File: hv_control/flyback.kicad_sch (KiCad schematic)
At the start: 33 parts, among them Q1 FOD817A300, U30 FSL4110LR, U31 TL431MFDT

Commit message: Moving to new CCU8 implementation. Moved trace and @arm scripts to octave archive.
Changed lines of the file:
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@@
-(kicad_sch (version 20201015) (generator eeschema)
+(kicad_sch (version 20210126) (generator eeschema)
   (paper "A4")
   (junction (at 74.93 49.53) (diameter 1.016) (color 0 0 0 0))
@@
     (stroke (width 0) (type solid) (color 0 0 0 0))
   )
-  (wire (pts (xy 82.55 49.53) (xy 104.14 49.53))
-    (stroke (width 0) (type solid) (color 0 0 0 0))
-  )
   (wire (pts (xy 82.55 63.5) (xy 82.55 92.71))
     (stroke (width 0) (type solid) (color 0 0 0 0))
@@
     (stroke (width 0) (type solid) (color 0 0 0 0))
   )
+  (wire (pts (xy 104.14 49.53) (xy 82.55 49.53))
+    (stroke (width 0) (type solid) (color 0 0 0 0))
+  )
   (wire (pts (xy 104.14 49.53) (xy 104.14 53.34))
     (stroke (width 0) (type solid) (color 0 0 0 0))
@@
     (stroke (width 0) (type solid) (color 0 0 0 0))
   )
-  (wire (pts (xy 196.85 143.51) (xy 209.55 143.51))
-    (stroke (width 0) (type solid) (color 0 0 0 0))
-  )
   (wire (pts (xy 200.66 49.53) (xy 195.58 49.53))
     (stroke (width 0) (type solid) (color 0 0 0 0))
@@
   )
   (wire (pts (xy 209.55 59.69) (xy 223.52 59.69))
+    (stroke (width 0) (type solid) (color 0 0 0 0))
+  )
+  (wire (pts (xy 209.55 143.51) (xy 196.85 143.51))
     (stroke (width 0) (type solid) (color 0 0 0 0))
   )
@@
       (effects (font (size 1.524 1.524)) hide)
     )
+    (pin "1")
+    (pin "2")
   )
   (symbol (lib_id "Device:R") (at 125.73 77.47 0) (unit 1)
@@
       (effects (font (size 1.27 1.27)) hide)
     )
+    (pin "1")
+    (pin "2")
   )
   (symbol (lib_id "Local:DIODE") (at 104.14 58.42 270) (mirror x) (unit 1)
@@
       (effects (font (size 1.27 1.27)) hide)
     )
+    (pin "A")
+    (pin "C")
   )
   (symbol (lib_id "Local:DIODE") (at 125.73 91.44 270) (unit 1)
@@
       (effects (font (size 1.27 1.27)) hide)
     )
+    (pin "A")
+    (pin "C")
   )
   (symbol (lib_id "Local:DIODE") (at 186.69 49.53 0) (unit 1)
@@
       (effects (font (size 1.524 1.524)) hide)
     )
+    (pin "A")
+    (pin "C")
   )
   (symbol (lib_id "Local:DIODE") (at 186.69 74.93 0) (mirror y) (unit 1)
@@
       (effects (font (size 1.524 1.524)) hide)
     )
+    (pin "A")
+    (pin "C")
   )
   (symbol (lib_id "Local:R") (at 74.93 57.15 0) (unit 1)
@@
       (effects (font (size 1.27 1.27)) hide)
     )
+    (pin "1")
+    (pin "2")
   )
   (symbol (lib_id "Local:R") (at 74.93 109.22 0) (unit 1)
@@
       (effects (font (size 1.524 1.524)))
     )
+    (pin "1")
+    (pin "2")
   )
   (symbol (lib_id "Local:R") (at 82.55 57.15 0) (unit 1)
@@
       (effects (font (size 1.27 1.27)) hide)
     )
+    (pin "1")
+    (pin "2")
   )
   (symbol (lib_id "Local:R") (at 104.14 73.66 0) (unit 1)
@@
       (effects (font (size 1.524 1.524)) hide)
     )
+    (pin "1")
+    (pin "2")
   )
   (symbol (lib_id "Local:R") (at 142.24 92.71 0) (unit 1)
@@
       (effects (font (size 1.524 1.524)))
     )
+    (pin "1")
+    (pin "2")
   )
   (symbol (lib_id "Local:R") (at 166.37 107.95 0) (unit 1)
@@
       (effects (font (size 1.524 1.524)))
     )
+    (pin "1")
+    (pin "2")
   )
   (symbol (lib_id "Local:R") (at 173.99 92.71 0) (unit 1)
@@
       (effects (font (size 1.524 1.524)))
     )
+    (pin "1")
+    (pin "2")
   )
   (symbol (lib_id "Local:R") (at 173.99 115.57 270) (unit 1)
@@
       (effects (font (size 1.524 1.524)))
     )
+    (pin "1")
+    (pin "2")
   )
   (symbol (lib_id "Local:R") (at 176.53 41.91 270) (unit 1)
@@
       (effects (font (size 1.524 1.524)))
     )
+    (pin "1")
+    (pin "2")
   )
   (symbol (lib_id "Local:R") (at 176.53 67.31 270) (unit 1)
@@
       (effects (font (size 1.524 1.524)))
     )
+    (pin "1")
+    (pin "2")
   )
   (symbol (lib_id "Local:R") (at 196.85 107.95 0) (unit 1)
@@
       (effects (font (size 1.524 1.524)))
     )
+    (pin "1")
+    (pin "2")
   )
   (symbol (lib_id "Local:R") (at 196.85 135.89 0) (unit 1)
@@
       (effects (font (size 1.524 1.524)))
     )
+    (pin "1")
+    (pin "2")
   )
   (symbol (lib_id "Device:CP") (at 147.32 109.22 0) (unit 1)
@@
       (effects (font (size 1.524 1.524)) hide)
     )
+    (pin "1")
+    (pin "2")
   )
   (symbol (lib_id "Device:CP") (at 218.44 92.71 0) (unit 1)
@@
       (effects (font (size 1.524 1.524)) hide)
     )
+    (pin "1")
+    (pin "2")
   )
   (symbol (lib_id "Device:CP") (at 223.52 54.61 0) (unit 1)
@@
       (effects (font (size 1.524 1.524)) hide)
     )
+    (pin "1")
+    (pin "2")
   )
   (symbol (lib_id "Device:CP") (at 226.06 64.77 0) (unit 1)
@@
       (effects (font (size 1.524 1.524)) hide)
     )
+    (pin "1")
+    (pin "2")
   )
   (symbol (lib_id "Local:C") (at 82.55 109.22 0) (unit 1)
@@
       (effects (font (size 1.524 1.524)) hide)
     )
+    (pin "1")
+    (pin "2")
   )
   (symbol (lib_id "Local:C") (at 92.71 109.22 0) (unit 1)
@@
       (effects (font (size 1.524 1.524)))
     )
+    (pin "1")
+    (pin "2")
   )
   (symbol (lib_id "Local:C") (at 95.25 73.66 0) (unit 1)
@@
       (effects (font (size 1.524 1.524)) hide)
     )
+    (pin "1")
+    (pin "2")
   )
   (symbol (lib_id "Local:C") (at 137.16 109.22 0) (unit 1)
@@
       (effects (font (size 1.524 1.524)))
     )
+    (pin "1")
+    (pin "2")
   )
   (symbol (lib_id "Local:C") (at 187.96 115.57 270) (unit 1)
@@
       (effects (font (size 1.524 1.524)))
     )
+    (pin "1")
+    (pin "2")
   )
   (symbol (lib_id "Local:C") (at 189.23 41.91 270) (mirror x) (unit 1)
@@
       (effects (font (size 1.524 1.524)))
     )
+    (pin "1")
+    (pin "2")
   )
   (symbol (lib_id "Local:C") (at 189.23 67.31 270) (mirror x) (unit 1)
@@
       (effects (font (size 1.524 1.524)))
     )
+    (pin "1")
+    (pin "2")
   )
   (symbol (lib_id "Local:OPTO") (at 161.29 92.71 0) (mirror y) (unit 1)
@@
       (effects (font (size 1.27 1.27)) hide)
     )
+    (pin "1")
+    (pin "2")
+    (pin "3")
+    (pin "4")
   )
   (symbol (lib_id "Local:trafo_4") (at 162.56 58.42 0) (unit 1)
@@
       (effects (font (size 1.27 1.27)) hide)
     )
+    (pin "1")
+    (pin "10")
+    (pin "2")
+    (pin "4")
+    (pin "6")
+    (pin "7")
+    (pin "8")
+    (pin "9")
   )
   (symbol (lib_id "Local:TL431") (at 166.37 128.27 0) (unit 1)
@@
       (effects (font (size 1.524 1.524)) hide)
     )
+    (pin "1")
+    (pin "2")
+    (pin "3")
   )
   (symbol (lib_id "Local:FSL4110LR") (at 106.68 97.79 0) (unit 1)
@@
       (effects (font (size 1.27 1.27)) hide)
     )
+    (pin "1")
+    (pin "2")
+    (pin "3")
+    (pin "4")
+    (pin "5")
+    (pin "7")
+    (pin "8")
   )
 )

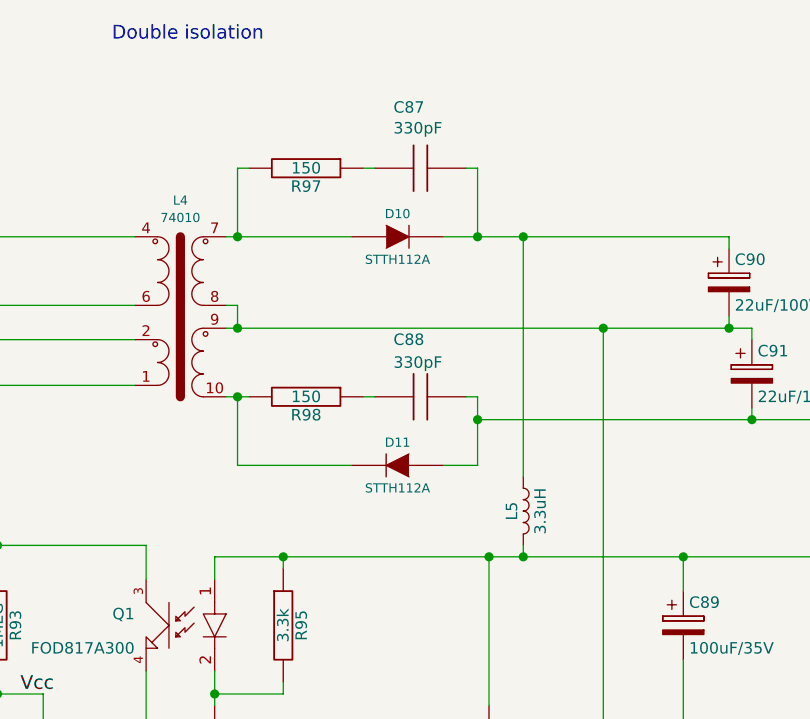
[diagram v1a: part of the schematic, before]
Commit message: MFS13 encoder using new uart driver.
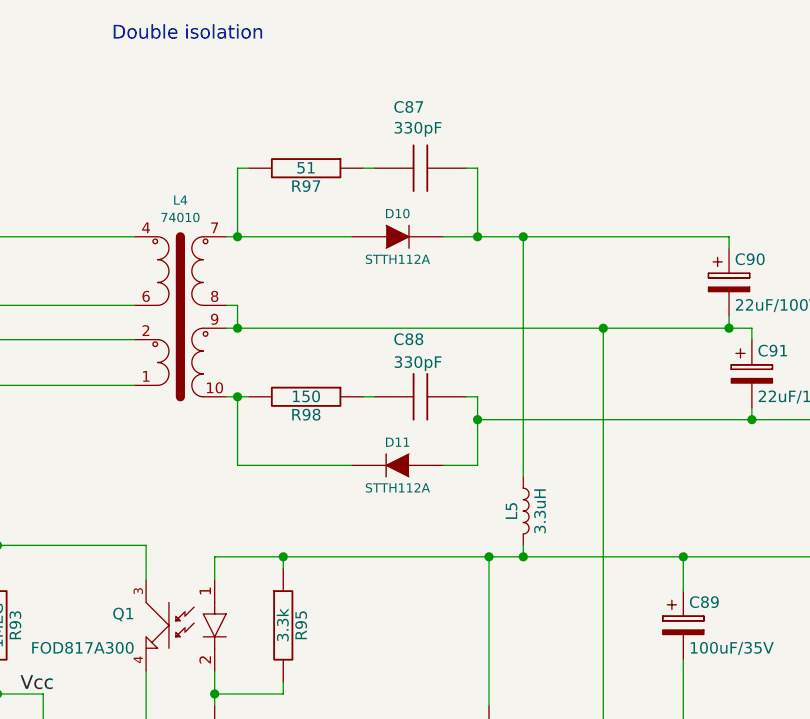
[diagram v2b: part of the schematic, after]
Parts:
- R97: value 150 -> 51
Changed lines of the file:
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@@
-    (stroke (width 0) (type solid) (color 0 0 0 0))
-  )
-  (wire (pts (xy 196.85 85.09) (xy 200.66 85.09))
     (stroke (width 0) (type solid) (color 0 0 0 0))
   )
@@
   )
   (wire (pts (xy 200.66 83.82) (xy 200.66 85.09))
+    (stroke (width 0) (type solid) (color 0 0 0 0))
+  )
+  (wire (pts (xy 200.66 85.09) (xy 196.85 85.09))
     (stroke (width 0) (type solid) (color 0 0 0 0))
   )
@@
     (in_bom yes) (on_board yes)
     (property "Reference" "R97" (id 0) (at 176.53 43.942 90))
-    (property "Value" "150" (id 1) (at 176.53 41.91 90))
+    (property "Value" "51" (id 1) (at 176.53 41.91 90))
     (property "Footprint" "Resistor_SMD:R_0603_1608Metric" (id 2) (at 176.53 41.91 0)
       (effects (font (size 1.524 1.524)) hide)

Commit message: Ordered new boards.
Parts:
- D10, D11, D8, D9: value STTH112A -> ${SIM.PARAMS}; Spice_Node_Sequence A,C -> (none)
- Q1: value FOD817A300 -> TCLT1003; footprint Package_DIP:DIP-4_W7.62mm -> Package_SO:SOP-4_3.8x7.5mm_P2.54mm; Digikey FOD817A300-ND -> (none); Farnell 2453196 -> (none); Manufacturer ON -> Vishay; Mouser 512-FOD817A -> (none); PartNr FOD817A300 -> TCLT1003; domain 3,4-1,2=3.2 -> 3,4-1,2=5.5; ec_mfg (none) -> Vishay; ec_mpn (none) -> TCLT1003
- R100: value 24k -> 39k
- U31: value TL431MFDT -> ${SIM.PARAMS}; Spice_Node_Sequence 3,2,1 -> (none)
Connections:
- net VOLTAGE: now reaches C86.1, R100.1, R99.2, U31.1 (ref)

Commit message: Remarks for next version.
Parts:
- C85, C90, C91: value 22uF/100V -> 100uF/35V; Mouser 667-EEE-1HA220WP -> (none); PartNr EEE-1HA220WP -> EEEFK1V101P
- C89: Mouser 667-EEE-1HA220WP -> (none); PartNr EEE-1HA220WP -> EEEFK1V101P
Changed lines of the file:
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@@
       (effects (font (size 1.27 1.27)) (justify left))
     )
-    (property "Value" "22uF/100V" (at 147.955 111.76 0)
+    (property "Value" "100uF/35V" (at 147.955 111.76 0)
       (effects (font (size 1.27 1.27)) (justify left))
     )
@@
       (effects (font (size 1.524 1.524)) hide)
     )
-    (property "PartNr" "EEE-1HA220WP" (at 147.32 109.22 0)
-      (effects (font (size 1.524 1.524)) hide)
-    )
-    (property "Mouser" "667-EEE-1HA220WP" (at 147.32 109.22 0)
+    (property "PartNr" "EEEFK1V101P" (at 147.32 109.22 0)
+      (effects (font (size 1.524 1.524)) hide)
+    )
+    (property "Mouser" "" (at 147.32 109.22 0)
       (effects (font (size 1.524 1.524)) hide)
     )
@@
       (effects (font (size 1.27 1.27)) (justify left))
     )
-    (property "Value" "22uF/100V" (at 224.155 57.15 0)
+    (property "Value" "100uF/35V" (at 224.155 57.15 0)
       (effects (font (size 1.27 1.27)) (justify left))
     )
@@
       (effects (font (size 1.524 1.524)) hide)
     )
-    (property "PartNr" "EEE-1HA220WP" (at 223.52 54.61 0)
-      (effects (font (size 1.524 1.524)) hide)
-    )
-    (property "Mouser" "667-EEE-1HA220WP" (at 223.52 54.61 0)
+    (property "PartNr" "EEEFK1V101P" (at 223.52 54.61 0)
+      (effects (font (size 1.524 1.524)) hide)
+    )
+    (property "Mouser" "" (at 223.52 54.61 0)
       (effects (font (size 1.524 1.524)) hide)
     )
@@
       (effects (font (size 1.27 1.27)) (justify left))
     )
-    (property "Value" "22uF/100V" (at 226.695 67.31 0)
+    (property "Value" "100uF/35V" (at 226.695 67.31 0)
       (effects (font (size 1.27 1.27)) (justify left))
     )
@@
       (effects (font (size 1.524 1.524)) hide)
     )
-    (property "PartNr" "EEE-1HA220WP" (at 226.06 64.77 0)
-      (effects (font (size 1.524 1.524)) hide)
-    )
-    (property "Mouser" "667-EEE-1HA220WP" (at 226.06 64.77 0)
+    (property "PartNr" "EEEFK1V101P" (at 226.06 64.77 0)
+      (effects (font (size 1.524 1.524)) hide)
+    )
+    (property "Mouser" "" (at 226.06 64.77 0)
       (effects (font (size 1.524 1.524)) hide)
     )
@@
       (effects (font (size 1.524 1.524)) hide)
     )
-    (property "PartNr" "EEE-1HA220WP" (at 218.44 92.71 0)
-      (effects (font (size 1.524 1.524)) hide)
-    )
-    (property "Mouser" "667-EEE-1HA220WP" (at 218.44 92.71 0)
-      (effects (font (size 1.524 1.524)) hide)
-    )
+    (property "PartNr" "EEEFK1V101P" (at 218.44 92.71 0)
+      (effects (font (size 1.524 1.524)) hide)
+    )
+    (property "Mouser" "" (at 218.44 92.71 0)
+      (effects (font (size 1.524 1.524)) hide)
+    )

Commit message: Adding cpuinfo.m
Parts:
- Q1: Mouser (none) -> 782-TCLT1003
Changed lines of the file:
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@@
       (effects (font (size 1.27 1.27)) hide)
     )
-    (property "Mouser" "" (at 0 185.42 0)
+    (property "Mouser" "782-TCLT1003" (at 0 185.42 0)
       (effects (font (size 1.27 1.27)) hide)
     )

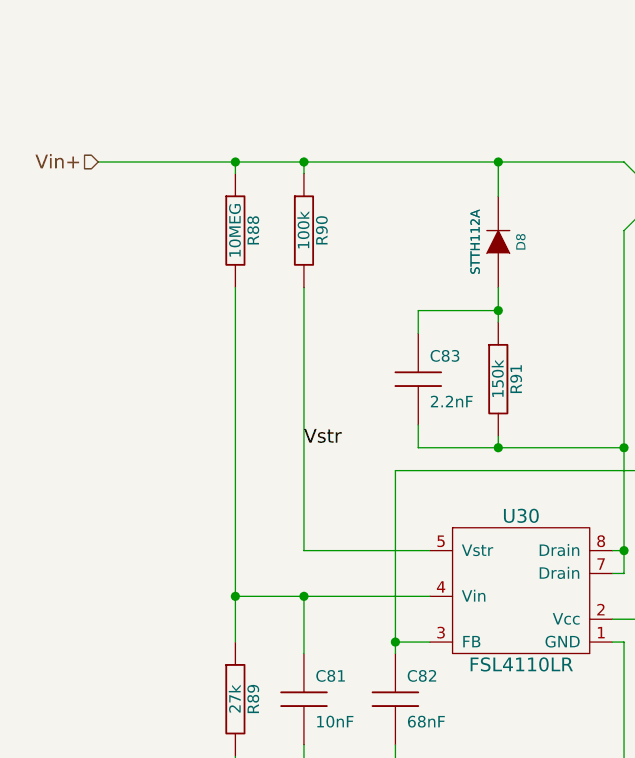
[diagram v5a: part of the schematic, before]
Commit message: Allow for negated index pulse on linear encoder.
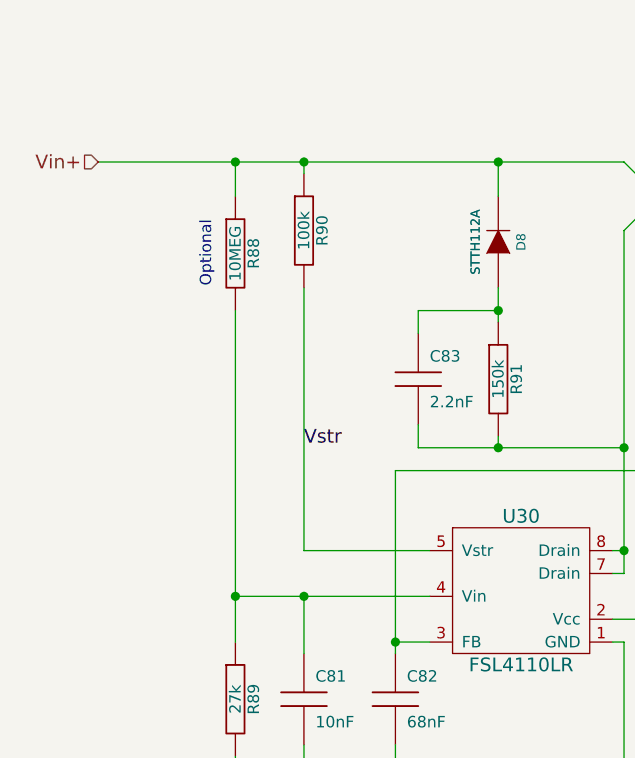
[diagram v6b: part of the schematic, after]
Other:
- note added: "Optional"
- moved on the sheet: R88
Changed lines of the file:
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@@
     (stroke (width 0) (type solid))
   )
-  (wire (pts (xy 74.93 49.53) (xy 74.93 50.8))
+  (wire (pts (xy 74.93 49.53) (xy 74.93 53.34))
     (stroke (width 0) (type solid))
   )
@@
     (stroke (width 0) (type solid))
   )
-  (wire (pts (xy 74.93 63.5) (xy 74.93 97.79))
+  (wire (pts (xy 74.93 66.04) (xy 74.93 97.79))
     (stroke (width 0) (type solid))
   )
@@
   (text "4.7k -> 6.2k for Cree FETS" (at 181.61 148.59 0)
     (effects (font (size 1.524 1.524)) (justify left bottom))
+  )
+  (text "Optional" (at 72.39 63.5 90)
+    (effects (font (size 1.27 1.27)) (justify left bottom))
   )
   (label "Vstr" (at 82.55 81.28 0) (fields_autoplaced)
@@
     )
   )
-  (symbol (lib_id "Local:R") (at 74.93 57.15 0) (unit 1)
-    (in_bom yes) (on_board yes) (dnp no)
-    (property "Reference" "R88" (at 76.962 57.15 90)
+  (symbol (lib_id "Local:R") (at 74.93 59.69 0) (unit 1)
+    (in_bom yes) (on_board yes) (dnp no)
+    (property "Reference" "R88" (at 76.962 59.69 90)
       (effects (font (size 1.27 1.27)))
     )
-    (property "Value" "10MEG" (at 74.93 57.15 90)
+    (property "Value" "10MEG" (at 74.93 59.69 90)
       (effects (font (size 1.27 1.27)))
     )
-    (property "Footprint" "Resistor_SMD:R_1206_3216Metric" (at 74.93 57.15 0)
-      (effects (font (size 1.524 1.524)) hide)
-    )
-    (property "Datasheet" "" (at 74.93 57.15 0)
+    (property "Footprint" "Resistor_SMD:R_1206_3216Metric" (at 74.93 59.69 0)
+      (effects (font (size 1.524 1.524)) hide)
+    )
+    (property "Datasheet" "" (at 74.93 59.69 0)
       (effects (font (size 1.524 1.524)))
     )
-    (property "Farnell" "2470930" (at 74.93 57.15 0)
-      (effects (font (size 1.524 1.524)) hide)
-    )
-    (property "Digikey" "CHV1206-FX-1005ELFCT-ND" (at 74.93 57.15 0)
+    (property "Farnell" "2470930" (at 74.93 59.69 0)
+      (effects (font (size 1.524 1.524)) hide)
+    )
+    (property "Digikey" "CHV1206-FX-1005ELFCT-ND" (at 74.93 59.69 0)
       (effects (font (size 1.27 1.27)) hide)
     )
-    (property "domain" "1-2=1.3" (at 74.93 57.15 90)
+    (property "domain" "1-2=1.3" (at 74.93 59.69 90)
       (effects (font (size 1.27 1.27)) hide)
     )
